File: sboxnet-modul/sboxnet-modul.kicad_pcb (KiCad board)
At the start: 2 copper layers, 62 x 62.4 mm, 39 parts, among them J1 Conn_01x03, J2 Conn_02x03_Odd_Even, J3 Conn_01x04_Female, J4 8P8C, J5 8P8C, J6 sboxnet-buchse_2x17, SW1 SW_Push, U1 MCP1703A-3302_SOT223, U2 MCP1703A-5002_SOT223, U3 SN65HVD230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

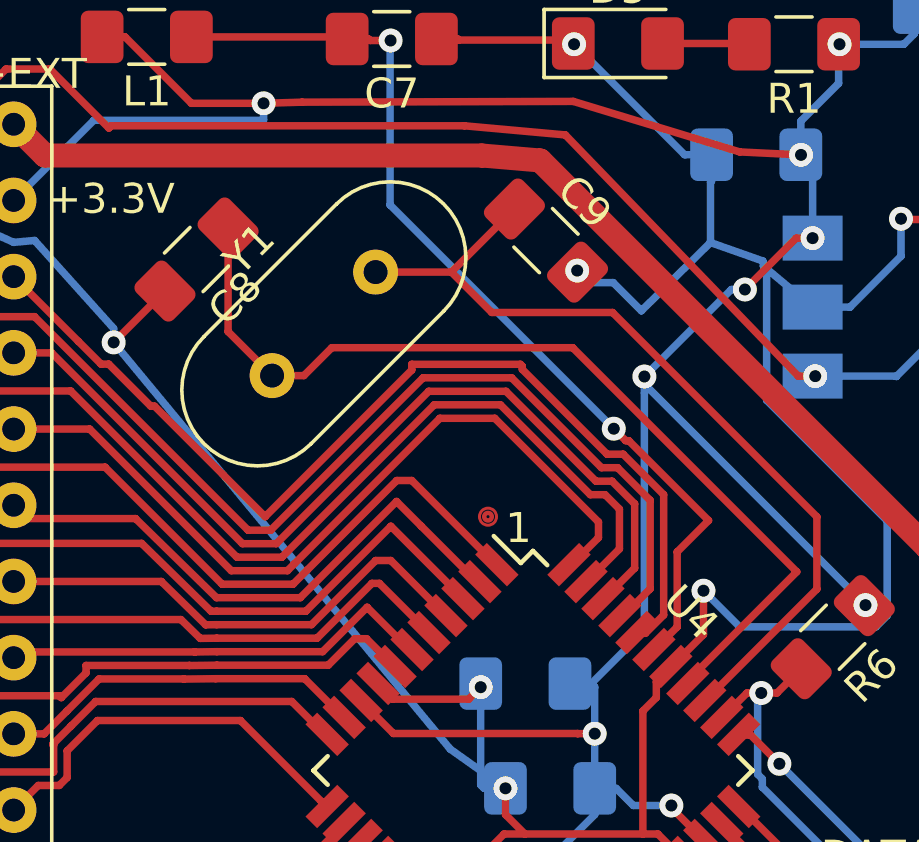
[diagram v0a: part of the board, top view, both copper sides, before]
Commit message: QS4A_0303S1.5UP footprint
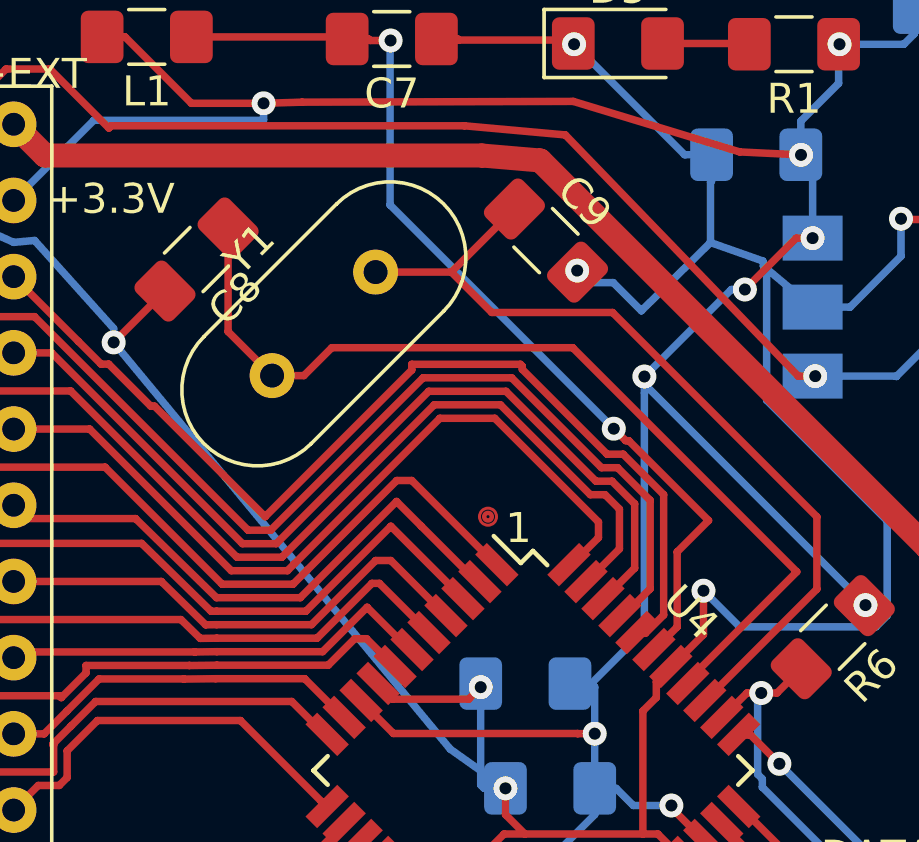
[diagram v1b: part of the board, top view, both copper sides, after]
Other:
- net class Default removed

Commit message: sboxnet-modul v5
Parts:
- removed J3: Conn_01x04_Female, Connector_PinHeader_2.54mm:PinHeader_1x04_P2.54mm_Vertical
- C3: value 10u -> +10u
- D5: value LED -> bl +
- U1 3.3v: renamed from U1
- U2 5v: renamed from U2; moved to F.Cu
- moved U2 5v 10.3 mm to (126.8, 81.2), turned to 180 degrees
- moved R2 9.17 mm to (134.2, 118.8)
- moved J5 9.02 mm to (138.5, 109.3)
- moved Rx3 9.02 mm to (146.2, 120.8)
- moved buchse 7.52 mm to (94.2, 120.8)
- moved J4 7.03 mm to (138.5, 93.6)
- moved D2 6.69 mm to (104.2, 120.5)
- moved D3 6.64 mm to (98.5, 120.5)
- moved R4 5.95 mm to (101.0, 115.0)
- moved J1 5.76 mm to (144.0, 82.8)
- moved SW1 5.70 mm to (114.0, 119.8)
- moved U3 5.69 mm to (127.0, 120.5)
- moved D1 5.65 mm to (143.8, 78.5)
- moved R3 5.36 mm to (104.2, 115.0)
- moved Rx2 4.88 mm to (146.2, 71.0)
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- renumbered R to Rx1, R to Rx2, R to Rx3
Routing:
- net GND: track 275.8 -> 18.9 mm, vias 13 -> 17
- net DCC_B: track 77.3 -> 57.0 mm, vias 2 -> 0
- net +3V3: track 171.1 -> 188.9 mm, vias 13 -> 1
- net PDICLK: track 38.8 -> 21.6 mm, vias 1 -> 0
- net +7V: track 54.3 -> 40.0 mm, vias 1 -> 0
- net CANH: track 44.7 -> 31.2 mm, vias 1 -> 0
- net +5V: track 65.7 -> 53.5 mm, vias 2 -> 1
- net PDI_DATA: track 23.9 -> 12.1 mm, vias 1 -> 0
- net CANL: track 38.0 -> 30.0 mm, vias 1 -> 0
- net PA0: track 34.2 -> 26.3 mm, vias 0 -> 1
- net DCC_A: track 69.6 -> 61.8 mm, vias 3 -> 0
- net Net-(C8-Pad1): track 31.8 -> 24.3 mm, vias 0 -> 1
- net Net-(U3-Pad4): track 35.3 -> 28.0 mm, vias 2 -> 0
- net PA2: track 30.6 -> 23.9 mm, vias 0 -> 1
- net PE0: track 30.3 -> 23.8 mm
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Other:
- board size 62 x 62.4 mm -> 57 x 54.7 mm
- board text added: "03.01.23"
- board text added: "Sboxnet Modul V5"
- board text added: "data"
- board text removed: "+bl"
- board text removed: "25.03.2021"
- board text removed: "DATA"
- board text removed: "Sboxnet Modul V4"

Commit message: restruktur
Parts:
- removed C1, C10, C4, C5, C6: 100n, Capacitor_SMD:C_1206_3216Metric_Pad1.42x1.75mm_HandSolder
- removed C2: 10u, Capacitor_SMD:C_1206_3216Metric_Pad1.42x1.75mm_HandSolder
- removed C3: +10u, Capacitor_SMD:C_1206_3216Metric
- removed C7: 1u, Capacitor_SMD:C_1206_3216Metric_Pad1.42x1.75mm_HandSolder
- removed C8, C9: 15p, Capacitor_SMD:C_1206_3216Metric_Pad1.42x1.75mm_HandSolder
- removed D1: SKL13B, Diode_SMD:D_SMB_Handsoldering
- removed D2, D3, D4: LED, LED_SMD:LED_1206_3216Metric_Pad1.42x1.75mm_HandSolder
- removed D5: bl +, LED_SMD:LED_1206_3216Metric_Pad1.42x1.75mm_HandSolder
- removed J1: Conn_01x03, Connector_PinHeader_2.54mm:PinHeader_1x03_P2.54mm_Vertical
- removed J2: Conn_02x03_Odd_Even, sboxnet:wannenstecker_gerade_6pin
- removed J4, J5: 8P8C, sboxnet:8p8c-mebp
- removed L1: Ferrit 60Ohm, Inductor_SMD:L_1206_3216Metric_Pad1.42x1.75mm_HandSolder
- removed R1, R3, R4, R7: 470, Resistor_SMD:R_1206_3216Metric_Pad1.42x1.75mm_HandSolder
- removed R2: 0, Resistor_SMD:R_1206_3216Metric_Pad1.42x1.75mm_HandSolder
- removed R5: 1k, Resistor_SMD:R_1206_3216Metric_Pad1.42x1.75mm_HandSolder
- removed R6: 10k, Resistor_SMD:R_1206_3216Metric_Pad1.42x1.75mm_HandSolder
- removed Rx1, Rx2, Rx3, buchse: MH2.2, MountingHole:MountingHole_2.2mm_M2
- removed SW1: SW_Push, sboxnet:JTP-1130
- removed U1 3.3v: MCP1703A-3302_SOT223, Package_TO_SOT_SMD:SOT-223-3_TabPin2
- removed U2 5v: MCP1703A-5002_SOT223, Package_TO_SOT_SMD:SOT-223-3_TabPin2
- removed U3: SN65HVD230, Package_SO:SOIC-8_3.9x4.9mm_P1.27mm
- removed U4: ATxmega128A4U-AU, Package_QFP:TQFP-44_10x10mm_P0.8mm
- removed Y1: 16MHz, Crystal:Crystal_HC49-U_Vertical
- moved J6 9.81 mm to (86.3, 119.1)
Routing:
- net +3V3: track 188.9 -> 0.00 mm, vias 1 -> 0
- net DCC_A: track 61.8 -> 0.00 mm
- net DCC_B: track 57.0 -> 0.00 mm
- net +5V: track 53.5 -> 0.00 mm, vias 1 -> 0
- net +V: track 52.9 -> 0.00 mm
- net +7V: track 40.0 -> 0.00 mm
- net CANH: track 31.2 -> 0.00 mm
- net AVCC: track 31.2 -> 0.00 mm
- net CANL: track 30.0 -> 0.00 mm
- net PA1: track 29.3 -> 0.00 mm
- net PD7: track 28.9 -> 0.00 mm, vias 1 -> 0
- net Net-(U3-Pad4): track 28.0 -> 0.00 mm
- net PD5: track 27.3 -> 0.00 mm, vias 1 -> 0
- net PE1: track 27.0 -> 0.00 mm
- net PD6: track 26.8 -> 0.00 mm
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- removed copper zone on B.Cu, net GND
- removed copper zone on F.Cu, net GND
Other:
- board outline removed
- board text removed: "+"
- board text removed: "+10u"
- board text removed: "+3.3V"
- board text removed: "+7V"
- board text removed: "+EXT"
- board text removed: "+or"
- board text removed: "03.01.23"
- board text removed: "1"
- board text removed: "CLK"
- board text removed: "GND"
- board text removed: "Sboxnet Modul V5"
- board text removed: "Thomas Maier tom@tom.ist-im-web.de"
- board text removed: "data"
- board text removed: "gn"
- board text removed: "rt"

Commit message: fix
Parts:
- added C1: 100n, Capacitor_SMD:C_1206_3216Metric_Pad1.33x1.80mm_HandSolder, F.Cu at (163.1, 105.0)
- added C10: 100n, Capacitor_SMD:C_1206_3216Metric_Pad1.33x1.80mm_HandSolder, F.Cu at (157.1, 111.7)
- added C2: 10u, Capacitor_SMD:C_1206_3216Metric_Pad1.33x1.80mm_HandSolder, F.Cu at (163.1, 108.4)
- added C3: 10u, Capacitor_SMD:C_1206_3216Metric, F.Cu at (141.0, 101.0)
- added C4: 100n, Capacitor_SMD:C_1206_3216Metric_Pad1.33x1.80mm_HandSolder, F.Cu at (151.1, 115.1)
- added C5: 100n, Capacitor_SMD:C_1206_3216Metric_Pad1.33x1.80mm_HandSolder, F.Cu at (157.1, 108.4)
- added C6: 100n, Capacitor_SMD:C_1206_3216Metric_Pad1.33x1.80mm_HandSolder, F.Cu at (151.1, 111.7)
- added C7: 1u, Capacitor_SMD:C_1206_3216Metric_Pad1.33x1.80mm_HandSolder, F.Cu at (157.1, 105.0)
- added C8: 15p, Capacitor_SMD:C_1206_3216Metric_Pad1.33x1.80mm_HandSolder, F.Cu at (151.1, 105.0)
- added C9: 15p, Capacitor_SMD:C_1206_3216Metric_Pad1.33x1.80mm_HandSolder, F.Cu at (151.1, 108.4)
- added D1: SKL13B, Diode_SMD:D_SMB_Handsoldering, F.Cu at (144.1, 89.0)
- added D2: LED, LED_SMD:LED_1206_3216Metric_Pad1.42x1.75mm_HandSolder, F.Cu at (152.0, 80.6)
- added D3: LED, LED_SMD:LED_1206_3216Metric_Pad1.42x1.75mm_HandSolder, F.Cu at (133.4, 103.7)
- added D4: LED, LED_SMD:LED_1206_3216Metric_Pad1.42x1.75mm_HandSolder, F.Cu at (158.0, 80.6)
- added D5: LED, LED_SMD:LED_1206_3216Metric_Pad1.42x1.75mm_HandSolder, F.Cu at (152.3, 84.0)
- added J1: Conn_01x03, Connector_PinHeader_2.54mm:PinHeader_1x03_P2.54mm_Vertical, F.Cu at (135.8, 94.7)
- added J2: Conn_02x03_Odd_Even, sboxnet:wannenstecker_gerade_6pin, F.Cu at (142.4, 76.2)
- added J4: 8P8C, sboxnet:8p8c-mebp, F.Cu at (114.3, 81.3)
- added J5: 8P8C, sboxnet:8p8c-mebp, F.Cu at (130.7, 81.3)
- added L1: Ferrit 60Ohm, Inductor_SMD:L_1206_3216Metric_Pad1.42x1.75mm_HandSolder, F.Cu at (152.3, 87.3)
- added R1: 470, Resistor_SMD:R_1206_3216Metric_Pad1.30x1.75mm_HandSolder, F.Cu at (157.0, 115.1)
- added R2: 0, Resistor_SMD:R_1206_3216Metric_Pad1.30x1.75mm_HandSolder, F.Cu at (163.1, 111.7)
- added R3: 470, Resistor_SMD:R_1206_3216Metric_Pad1.30x1.75mm_HandSolder, F.Cu at (163.1, 115.0)
- added R4: 470, Resistor_SMD:R_1206_3216Metric_Pad1.30x1.75mm_HandSolder, F.Cu at (169.1, 108.3)
- added R5: 1k, Resistor_SMD:R_1206_3216Metric_Pad1.30x1.75mm_HandSolder, F.Cu at (169.0, 111.7)
- added R6: 10k, Resistor_SMD:R_1206_3216Metric_Pad1.30x1.75mm_HandSolder, F.Cu at (169.1, 105.0)
- added R7: 470, Resistor_SMD:R_1206_3216Metric_Pad1.30x1.75mm_HandSolder, F.Cu at (169.0, 115.0)
- added SW1: SW_Push, sboxnet:JTP-1130, F.Cu at (143.6, 95.6)
- added U1: MCP1703A-3302_SOT223, Package_TO_SOT_SMD:SOT-223-3_TabPin2, F.Cu at (125.5, 103.1)
- added U2: MCP1703A-5002_SOT223, Package_TO_SOT_SMD:SOT-223-3_TabPin2, F.Cu at (153.9, 74.8)
- added U3: SN65HVD230, Package_SO:SOIC-8_3.9x4.9mm_P1.27mm, F.Cu at (163.0, 73.9)
- added U4: ATxmega128A4U-AU, Package_QFP:TQFP-44_10x10mm_P0.8mm, F.Cu at (113.3, 99.6)
- added Y1: 16MHz, Crystal:Crystal_HC49-U_Vertical, F.Cu at (124.6, 95.7)
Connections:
- J6 pad 3: +3V3 -> +3.3V

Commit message: sboxnet modul v6.1
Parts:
- C10, C3, C4, C6, C7, C8, C9, D1, L1, R1, R7, U2: moved to B.Cu
- moved R4 85.4 mm to (83.8, 113.0), turned to -90 degrees
- moved C2 82.6 mm to (85.1, 81.3), turned to 90 degrees
- moved R3 76.7 mm to (86.4, 113.0), turned to -90 degrees
- moved R5 76.3 mm to (92.7, 111.8)
- moved D2 75.6 mm to (86.4, 118.1), turned to -90 degrees
- moved R7 73.7 mm to (104.1, 80.0), turned to 180 degrees
- moved C7 70.8 mm to (87.6, 91.4)
- moved U3 67.1 mm to (110.5, 115.6), turned to -90 degrees
- moved C10 66.1 mm to (92.7, 96.5), turned to 180 degrees
- moved L1 64.7 mm to (87.6, 88.9), turned to 180 degrees
- moved R6 61.9 mm to (109.2, 120.7), turned to 180 degrees
- moved R1 61.8 mm to (103.5, 84.2), turned to 180 degrees
- moved C4 60.8 mm to (92.4, 99.1), turned to 180 degrees
- moved U2 59.7 mm to (94.6, 81.3), turned to 180 degrees
- moved C6 59.2 mm to (92.7, 101.6), turned to 180 degrees
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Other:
- board outline added: 49.5 x 48.3 mm

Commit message: sboxnet modul v6.2
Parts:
- removed J1: Conn_01x03, Connector_PinHeader_2.54mm:PinHeader_1x03_P2.54mm_Vertical
- C1, C5, R3, R4, R5: moved to B.Cu
- moved C1 65.4 mm to (85.1, 81.3), turned to -90 degrees
- moved C5 29.6 mm to (103.2, 102.9)
- moved C7 13.1 mm to (100.3, 94.5), turned to 135 degrees
- moved D1 8.42 mm to (119.7, 83.8)
- moved J5 3.81 mm to (116.8, 83.8)
- moved L1 2.51 mm to (87.6, 86.4)
- moved R1 1.80 mm to (104.1, 82.5)
- moved D4 1.60 mm to (100.3, 82.2)
- moved C9 1.27 mm to (105.4, 94.7)
- moved C3 0.47 mm to (100.3, 81.3)
- turned R5 to 180 degrees

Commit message: sboxnet modul V6
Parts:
- C3: footprint Capacitor_SMD:C_1206_3216Metric -> Capacitor_SMD:C_1206_3216Metric_Pad1.33x1.80mm_HandSolder
- L1: value Ferrit 60Ohm -> Ferrit
- U1  3.3V: renamed from U1
- U2  5V: renamed from U2
- moved C1 29.2 mm to (114.2, 80.9), turned to 0 degrees
- moved C5 28.1 mm to (85.1, 81.4), turned to -90 degrees
- moved R6 7.73 mm to (116.8, 119.4)
- moved R2 3.81 mm to (115.9, 114.3)
- moved R1 3.25 mm to (103.8, 79.3)
- moved R4 3.10 mm to (83.8, 116.1)
- moved R3 3.07 mm to (86.4, 116.1)
- moved D1 2.26 mm to (122.0, 83.6), turned to -90 degrees
- moved R5 2.01 mm to (92.3, 113.7)
- moved R7 1.76 mm to (103.8, 81.7)
- moved SW1 1.45 mm to (92.2, 118.2)
- moved U3 1.32 mm to (110.4, 116.9)
- moved D3 1.07 mm to (83.9, 119.2)
- moved D2 1.07 mm to (86.4, 119.2)
- moved D5 0.83 mm to (100.8, 79.3)
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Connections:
- D1 pad 2: Net-(D1-Pad2) -> +7V
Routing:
- net GND: track 0.00 -> 180.1 mm, vias 0 -> 12
- net +3.3V: track 0.00 -> 140.5 mm, vias 0 -> 7
- net DCC_A: track 0.00 -> 65.7 mm
- net DCC_B: track 0.00 -> 65.1 mm
- net +7V: track 0.00 -> 48.9 mm
- net PDICLK: track 0.00 -> 43.3 mm, vias 0 -> 4
- net CANL: track 0.00 -> 41.9 mm, vias 0 -> 1
- net CANH: track 0.00 -> 40.9 mm, vias 0 -> 3
- net +5V: track 0.00 -> 33.3 mm, vias 0 -> 1
- net PD7: track 0.00 -> 28.8 mm
- net PA1: track 0.00 -> 27.4 mm
- net Net-(C1-Pad2): track 0.00 -> 26.6 mm
- net PA0: track 0.00 -> 26.2 mm
- net PD5: track 0.00 -> 24.9 mm
- net PA3: track 0.00 -> 23.6 mm
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- added copper zone on B.Cu, net GND
- added copper zone on F.Cu, net GND
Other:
- board size 49.5 x 48.3 mm -> 49.6 x 46.2 mm
- board text added: "16MHz"
- board text added: "470"
- board text added: "bl"
- board text added: "gn"
- board text added: "or"
- board text added: "rt"
- board text added: "sboxnet Modul V6"

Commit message: sboxnet Modul v6
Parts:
- moved C10 6.33 mm to (91.4, 102.7), turned to -45 degrees
- moved C6 5.14 mm to (89.3, 97.7), turned to -135 degrees
- moved C4 4.41 mm to (96.7, 100.0), turned to 45 degrees
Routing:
- net GND: track 180.1 -> 166.3 mm, vias 12 -> 15
- net +3.3V: track 140.5 -> 137.1 mm
